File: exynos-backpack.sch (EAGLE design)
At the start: 53 parts, among them IC1 MIC5335-SPYMT, IC2 TXS0108ERGY, IC3 LTC4352DD, IC4 LTC4352DD, IC5 LTC4352DD, Q1 SI7234DP, Q2 SI7234DP, Q3 SI7234DP

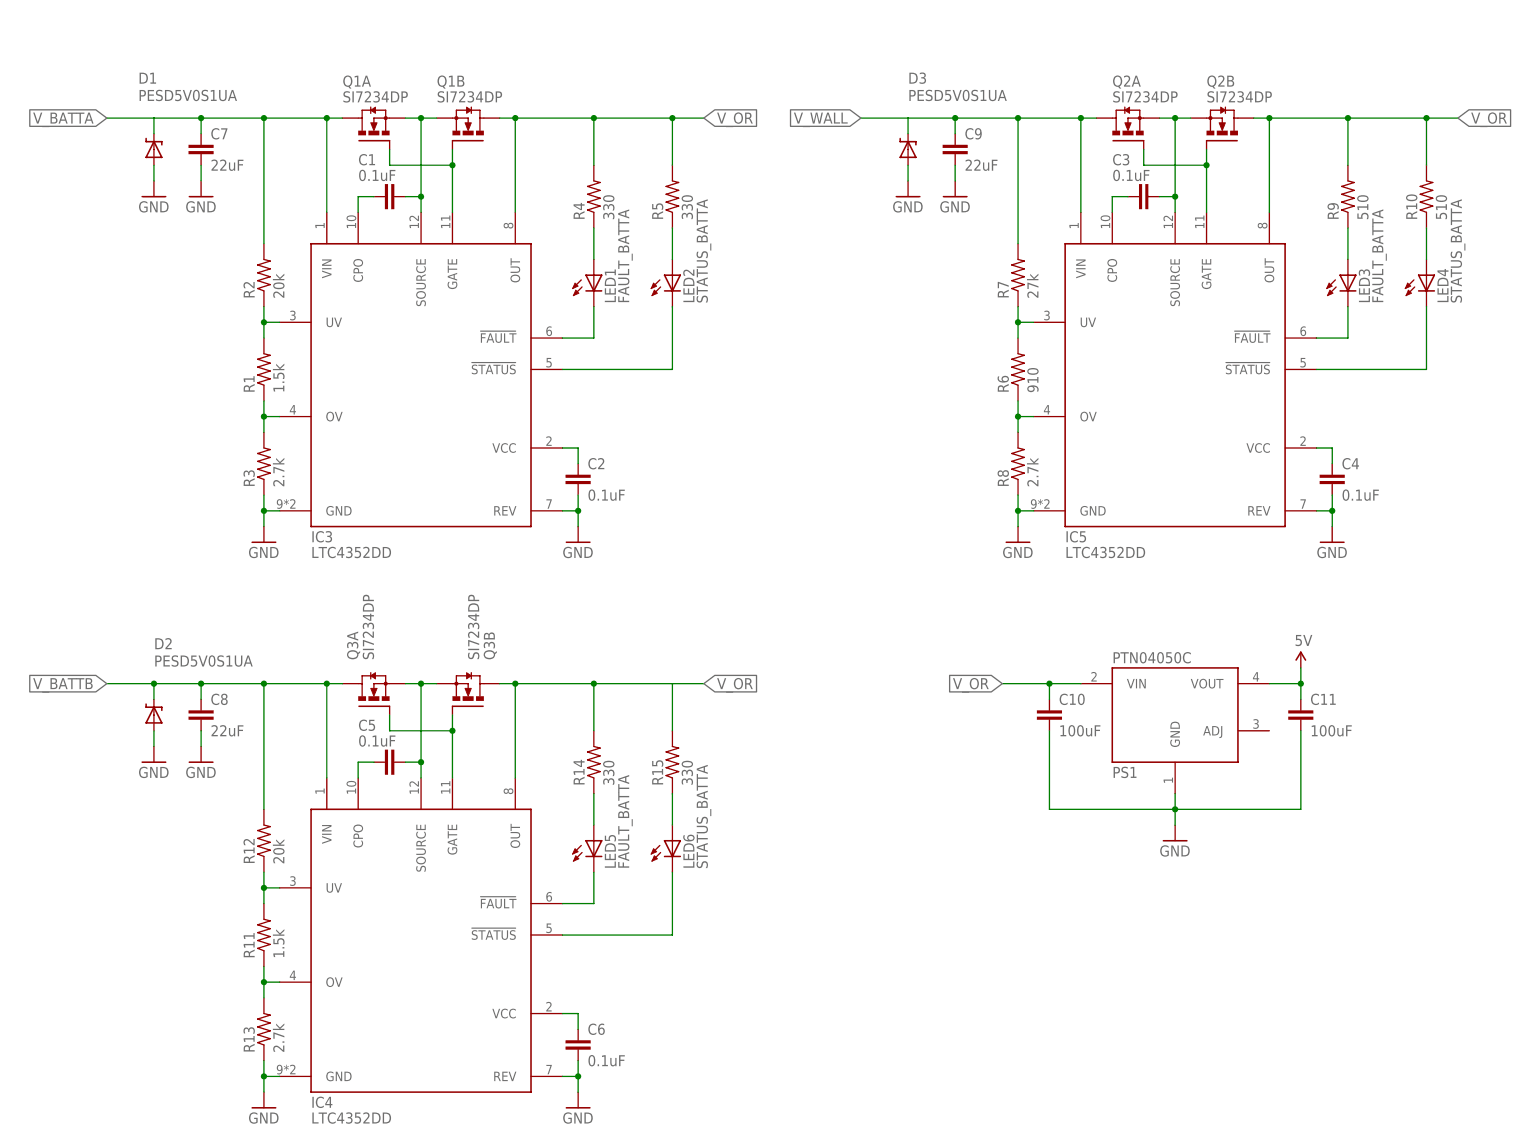
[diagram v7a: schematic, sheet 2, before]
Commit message: Rearrange LED circuits in schematic
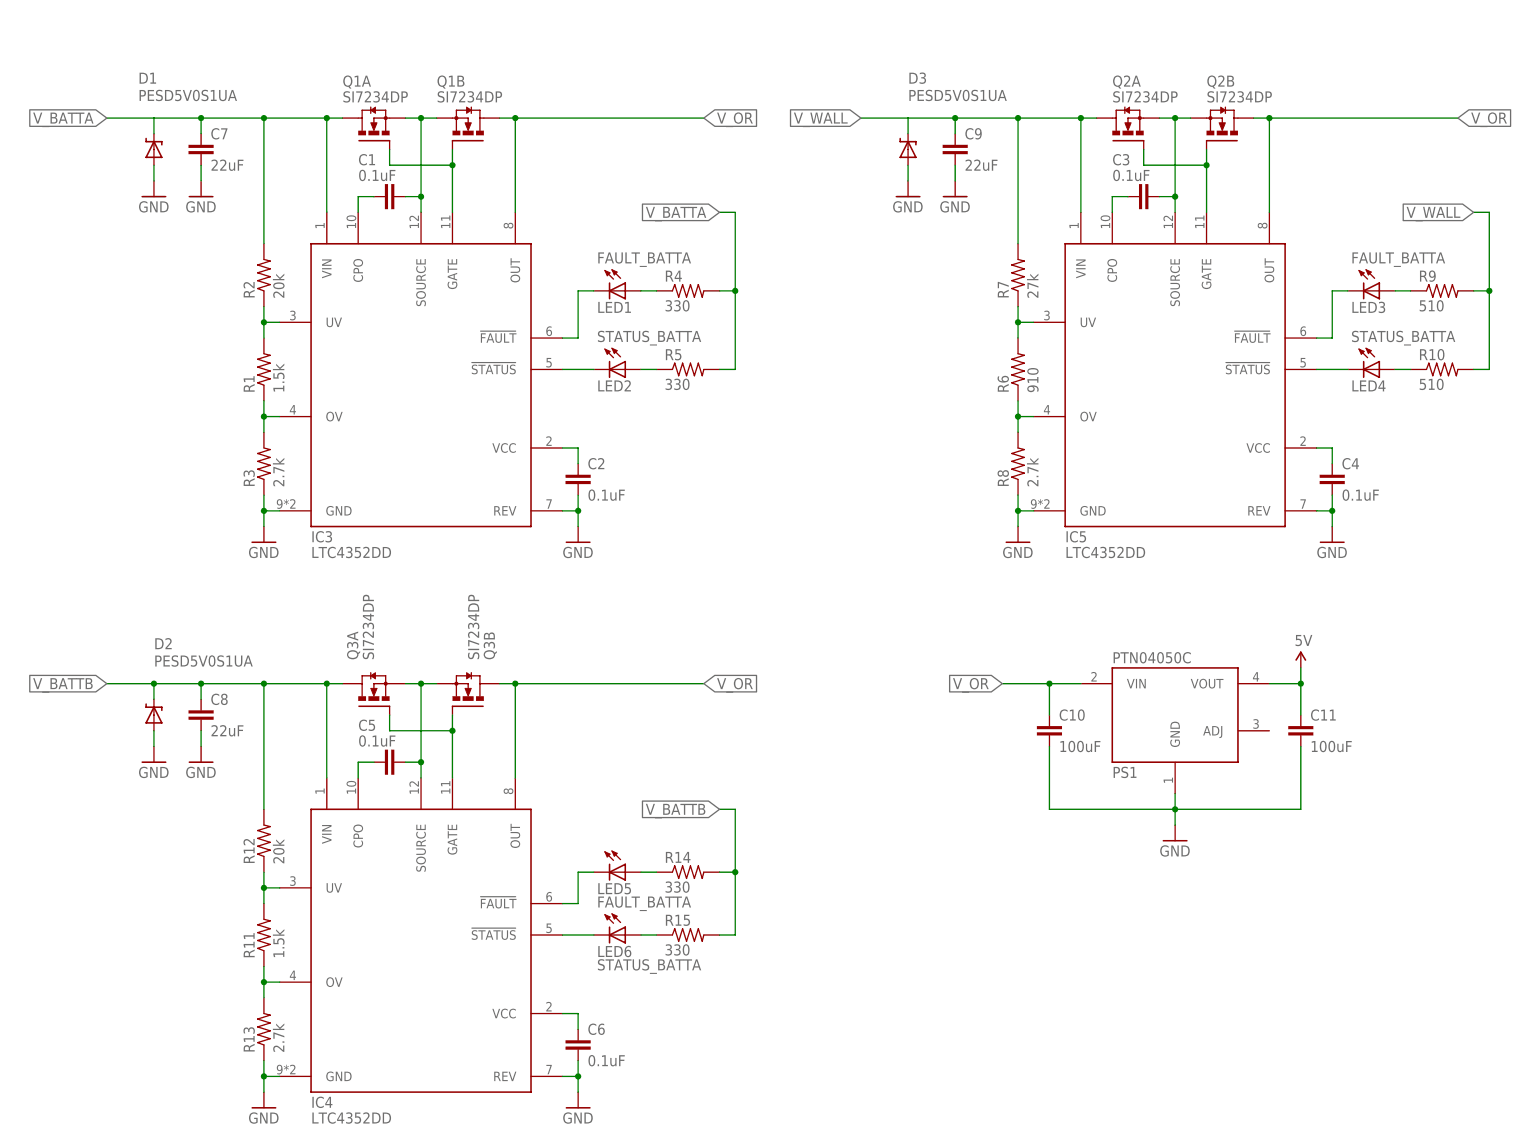
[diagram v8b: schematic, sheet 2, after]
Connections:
- net V_BATTA: now also R4.2, R5.2
- net V_BATTB: now also R14.2, R15.2
- net V_OR: no longer R10.2, R14.2, R15.2, R4.2, R5.2, R9.2
- net V_WALL: now also R10.2, R9.2
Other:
- moved on the sheet: C10, C11, LED1, LED2, LED3, LED4, LED5, LED6, R10, R14, R15, R4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
